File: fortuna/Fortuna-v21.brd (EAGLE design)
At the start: 66 x 55.9 mm, 41 parts, among them IC1 OPA4340P, J1 5V, J2 GND, J3 A0, J4 A3, J5 A5, J6 D2, J7 *D5, J8 *D10, J9 VIN, M1 MOTOR20MM, M2 MOTOR20MM, Q1 PN2222A, Q2 PN2222A

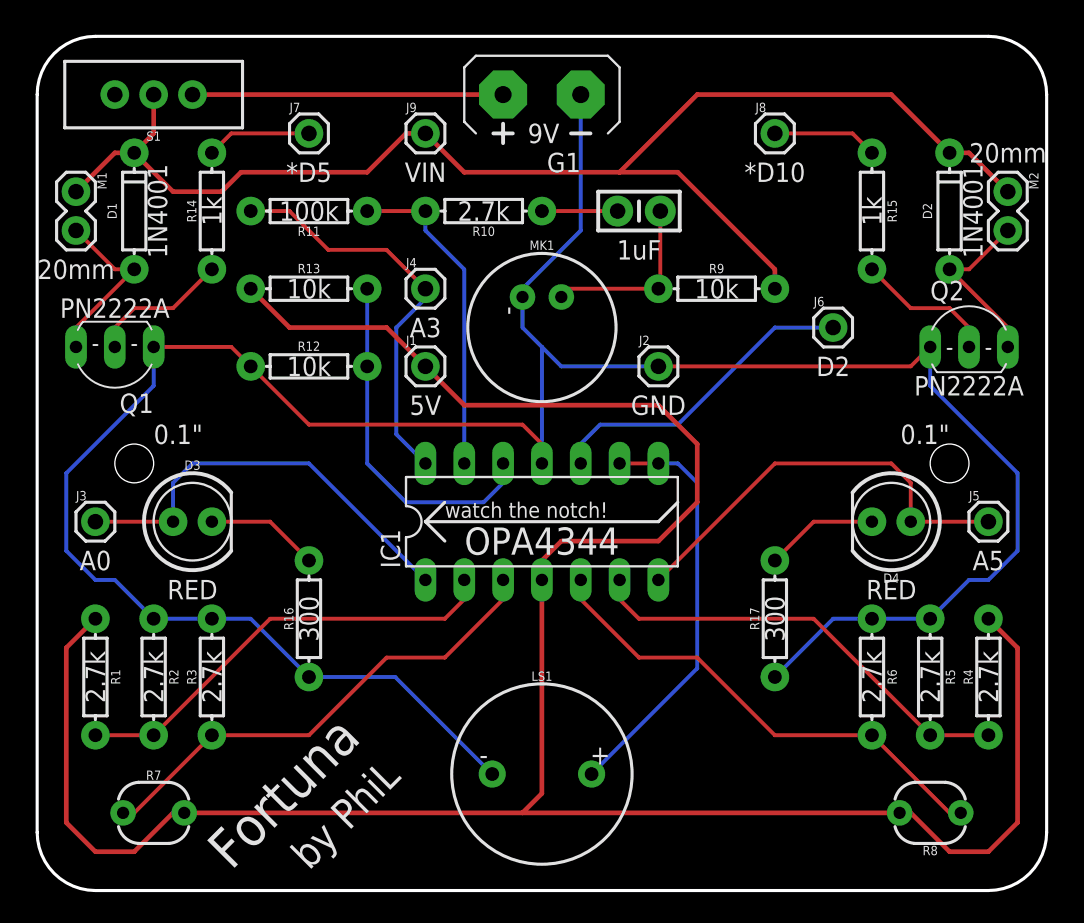
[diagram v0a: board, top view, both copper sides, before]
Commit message: Add GND to RATSNEST
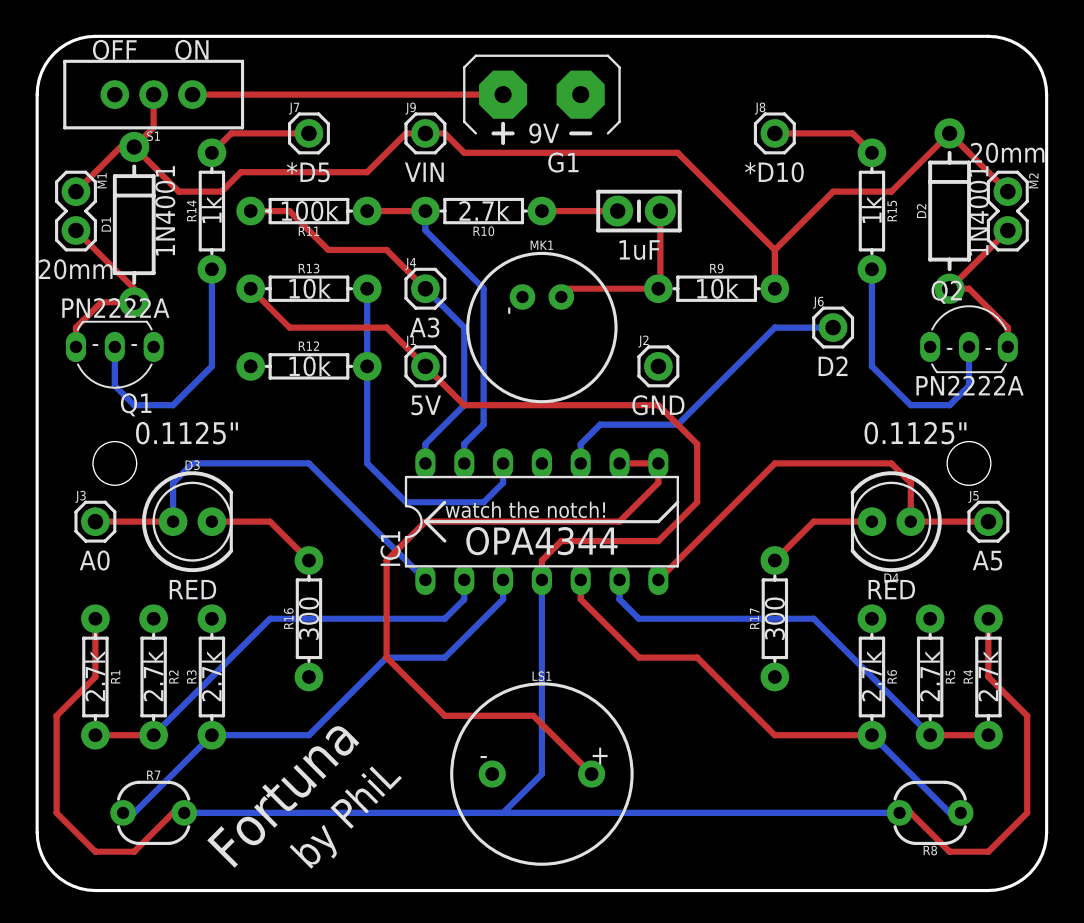
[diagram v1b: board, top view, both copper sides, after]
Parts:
- D1, D2: device SparkFun-DiscreteSemi:DIODE-1N4148 -> SparkFun-DiscreteSemi:DIODE-1N4001
- S1: value POWER_SWITCH -> ON/OFF
- moved D1 0.89 mm to (6.35, 43.6)
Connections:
- net VIN renamed VCC
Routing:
- net GND: track 166.6 -> 0.00 mm
- net OUT_BUZZER: track 27.5 -> 46.6 mm
- net VCC: track 88.8 -> 79.3 mm
- net N$9: track 9.20 -> 16.8 mm
- net N$14: track 9.20 -> 16.8 mm
- net 5V: track 160.2 -> 161.7 mm
- net OUT_MIC: track 26.5 -> 27.7 mm
- net -MIC: track 21.4 -> 22.4 mm
- net N$10: track 11.5 -> 12.0 mm
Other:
- board text added: "0.1125""
- board text added: "OFF"
- board text added: "ON"
- board text removed: "0.1""
